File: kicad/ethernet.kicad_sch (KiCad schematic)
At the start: 111 parts, among them J1 RJ45_Abracon_ARJP11A-MASA-B-A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, J2 Conn_Coaxial, J3 JTAG, J4 BATT, J5 Conn_Coaxial, J6 Conn_Coaxial, J7 POE, J8 POE+, J9 POE-, Q1 3904, Q10 3904, Q11 3904, Q12 3906, Q13 3904, Q2 3904, Q3 BSC340N08NS3G, Q4 MMBT5401L, Q5 3904, Q6 3906, Q7 3904, Q8 3906, Q9 3904, SW1 KSC701, U1 MSP432E401Y, U2 MAX-8Q, U3 TLV75733PDRV, U4 74AUC2G34, U5 74AUC2G34, U6 LM4040DBZ-2.5, U7 4N25, Y1 NX3225GA-25.000M-STD-CRG-2

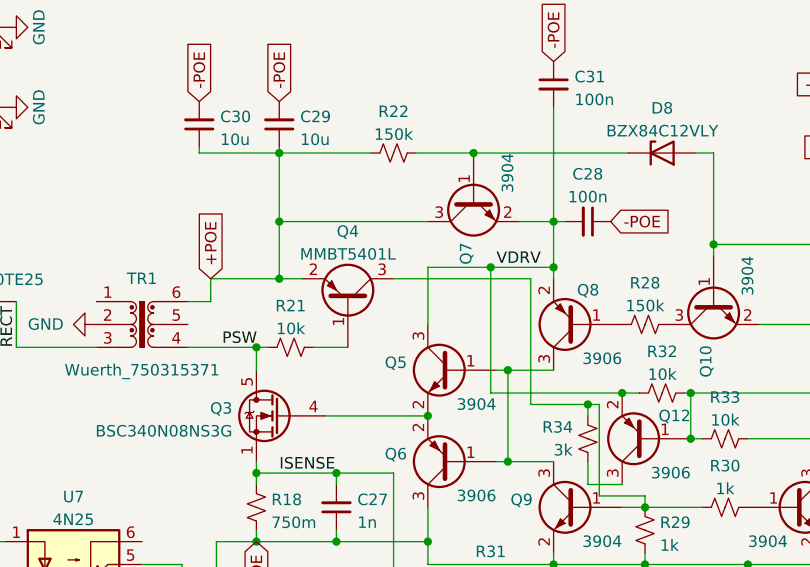
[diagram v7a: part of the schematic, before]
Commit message: migrating to C++
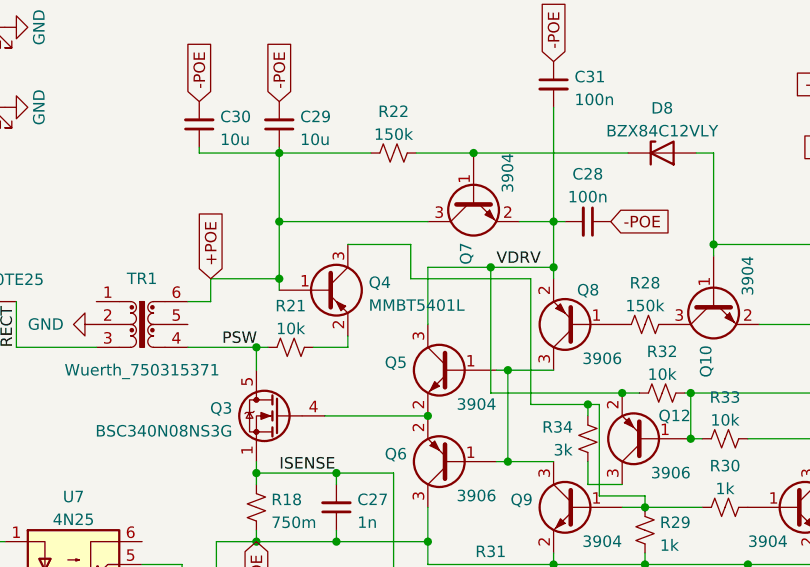
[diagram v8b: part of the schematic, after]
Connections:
- net +POE: now also Q4.1 (B); no longer Q4.2 (E)
- net at R21.1: now also Q4.2 (E); no longer Q4.1 (B)
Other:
- moved on the sheet: Q4
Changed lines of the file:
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@@
   (junction (at 158.75 165.1) (diameter 0) (color 0 0 0 0)
   )
+  (junction (at 330.2 186.69) (diameter 0) (color 0 0 0 0)
+  )
   (junction (at 90.17 144.78) (diameter 0) (color 0 0 0 0)
   )
@@
   (junction (at 163.83 38.1) (diameter 0) (color 0 0 0 0)
   )
-  (junction (at 330.2 186.69) (diameter 0) (color 0 0 0 0)
-  )
   (junction (at 158.75 129.54) (diameter 0) (color 0 0 0 0)
   )
@@
     (stroke (width 0) (type default) (color 0 0 0 0))
   )
+  (wire (pts (xy 330.2 186.69) (xy 330.2 187.96))
+    (stroke (width 0) (type default) (color 0 0 0 0))
+  )
   (wire (pts (xy 157.48 106.68) (xy 158.75 106.68))
     (stroke (width 0) (type default) (color 0 0 0 0))
@@
     (stroke (width 0) (type default) (color 0 0 0 0))
   )
+  (wire (pts (xy 337.82 182.88) (xy 344.805 182.88))
+    (stroke (width 0) (type default) (color 0 0 0 0))
+  )
   (wire (pts (xy 157.48 213.36) (xy 158.75 213.36))
     (stroke (width 0) (type default) (color 0 0 0 0))
@@
     (stroke (width 0) (type default) (color 0 0 0 0))
   )
-  (wire (pts (xy 330.2 186.69) (xy 332.74 186.69))
-    (stroke (width 0) (type default) (color 0 0 0 0))
-  )
   (wire (pts (xy 78.74 59.055) (xy 66.675 59.055))
     (stroke (width 0) (type default) (color 0 0 0 0))
@@
     (stroke (width 0) (type default) (color 0 0 0 0))
   )
-  (wire (pts (xy 342.9 186.69) (xy 358.14 186.69))
-    (stroke (width 0) (type default) (color 0 0 0 0))
-  )
   (wire (pts (xy 90.17 88.9) (xy 91.44 88.9))
     (stroke (width 0) (type default) (color 0 0 0 0))
@@
     (stroke (width 0) (type default) (color 0 0 0 0))
   )
+  (wire (pts (xy 334.01 194.31) (xy 337.82 194.31))
+    (stroke (width 0) (type default) (color 0 0 0 0))
+  )
   (wire (pts (xy 158.75 165.1) (xy 158.75 162.56))
     (stroke (width 0) (type default) (color 0 0 0 0))
@@
     (stroke (width 0) (type default) (color 0 0 0 0))
   )
+  (wire (pts (xy 344.805 182.88) (xy 344.805 186.69))
+    (stroke (width 0) (type default) (color 0 0 0 0))
+  )
   (wire (pts (xy 285.75 123.19) (xy 287.02 123.19))
     (stroke (width 0) (type default) (color 0 0 0 0))
@@
     (stroke (width 0) (type default) (color 0 0 0 0))
   )
-  (wire (pts (xy 334.01 194.31) (xy 337.82 194.31))
-    (stroke (width 0) (type default) (color 0 0 0 0))
-  )
   (wire (pts (xy 116.84 38.1) (xy 114.3 38.1))
     (stroke (width 0) (type default) (color 0 0 0 0))
@@
     (stroke (width 0) (type default) (color 0 0 0 0))
   )
+  (wire (pts (xy 358.14 186.69) (xy 344.805 186.69))
+    (stroke (width 0) (type default) (color 0 0 0 0))
+  )
   (wire (pts (xy 327.66 194.31) (xy 327.66 196.85))
     (stroke (width 0) (type default) (color 0 0 0 0))
@@
     (stroke (width 0) (type default) (color 0 0 0 0))
   )
+  (wire (pts (xy 337.82 193.04) (xy 337.82 194.31))
+    (stroke (width 0) (type default) (color 0 0 0 0))
+  )
   (wire (pts (xy 323.215 220.98) (xy 323.215 215.9))
     (stroke (width 0) (type default) (color 0 0 0 0))
@@
     (pin "1")
   )
-  (symbol (lib_id "Device:Q_PNP_BEC") (at 337.82 189.23 270) (mirror x) (unit 1)
+  (symbol (lib_id "Device:Q_PNP_BEC") (at 335.28 187.96 0) (unit 1)
     (in_bom yes) (on_board yes) (fields_autoplaced)
-    (property "Reference" "Q4" (id 0) (at 337.82 181.4408 90))
-    (property "Value" "MMBT5401L" (id 1) (at 337.82 183.9777 90))
-    (property "Footprint" "Package_TO_SOT_SMD:SOT-23" (id 2) (at 340.36 184.15 0)
+    (property "Reference" "Q4" (id 0) (at 340.1314 187.1253 0)
+      (effects (font (size 1.27 1.27)) (justify left))
+    )
+    (property "Value" "MMBT5401L" (id 1) (at 340.1314 189.6622 0)
+      (effects (font (size 1.27 1.27)) (justify left))
+    )
+    (property "Footprint" "Package_TO_SOT_SMD:SOT-23" (id 2) (at 340.36 185.42 0)
       (effects (font (size 1.27 1.27)) hide)
     )
-    (property "Datasheet" "~" (id 3) (at 337.82 189.23 0)
+    (property "Datasheet" "~" (id 3) (at 335.28 187.96 0)
       (effects (font (size 1.27 1.27)) hide)
     )
